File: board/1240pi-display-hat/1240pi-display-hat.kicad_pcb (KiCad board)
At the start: 2 copper layers, 34.3 x 71.1 mm, 8 parts, among them J1 Conn_02x05_Odd_Even, P208 Header, P415 Header, U1 74F126, U208 74F04, U415 74S74

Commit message: Switch hat boards from IDC ribbons to flat flex cables.
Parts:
- J1: value Conn_02x05_Odd_Even -> SFV10R-1ST; footprint Connector_PinHeader_2.54mm:PinHeader_2x05_P2.54mm_Vertical -> 0Local:Amphenol_SFV10R-1ST
- moved J1 5.64 mm to (104.0, 77.5), turned to -90 degrees
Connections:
- J1 pad 1: GND -> /~{EXT_EN}
- J1 pad 10: /~{VDRIVE} -> GND
- J1 pad 2: /~{EXT_EN} -> GND
- J1 pad 3: GND -> /PIX_CLK
- J1 pad 4: /PIX_CLK -> GND
- J1 pad 5: GND -> /VIDEO
- J1 pad 6: /VIDEO -> GND
- J1 pad 7: GND -> /~{HDRIVE}
- J1 pad 8: /~{HDRIVE} -> GND
- J1 pad 9: GND -> /~{VDRIVE}
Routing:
- net GND: track 106.3 -> 119.7 mm
- net /VIDEO: track 23.0 -> 19.2 mm, vias 0 -> 1
- net /PIX_CLK: track 30.6 -> 32.6 mm, vias 0 -> 1
- net /~{HDRIVE}: track 42.2 -> 43.8 mm
- net /~{EXT_EN}: track 41.2 -> 39.7 mm
- net /~{VDRIVE}: track 33.1 -> 33.9 mm, vias 0 -> 1
- net Net-(U1-Pad5): track 23.2 -> 23.7 mm
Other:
- board text added: "1240-Pi Display Board Mod v${REVISION}"
- board text added: "https://github.com/Elemecca/1240pi Licensed under CERN-OHL-S v2"
- board text removed: "1240-Pi Display Board Mod"
- board text removed: "GND"
- board text removed: "PIX_CLK"
- board text removed: "VIDEO"
- board text removed: "https://github.com/Elemecca/1240pi Licensed under CERN-OHL-P v2"
- board text removed: "~{EXT_EN}"
- board text removed: "~{HDRIVE}"
- board text removed: "~{VDRIVE}"

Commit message: Update board license to CERN-OHL-S v2+.
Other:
- board text added: "https://github.com/Elemecca/1240pi Licensed under CERN-OHL-S v2+"
- board text removed: "https://github.com/Elemecca/1240pi Licensed under CERN-OHL-S v2"
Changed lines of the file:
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@@
     (date "2022-05-21")
     (rev "1.0")
-    (company "© 2022 Sam Hanes, licensed under CERN-OHL-S v2")
+    (company "© 2022 Sam Hanes, licensed under CERN-OHL-S v2+")
     (comment 1 "https://github.com/Elemecca/1240pi")
-    (comment 4 "AISLER Project ID: DTIQIXZI")
   )
   (layers
@@
     (effects (font (size 1.2192 1.2192) (thickness 0.2032)) (justify left))
   )
-  (gr_text "https://github.com/Elemecca/1240pi\nLicensed under CERN-OHL-S v2" (at 125.73 59.69 -90) (layer "F.SilkS")
+  (gr_text "https://github.com/Elemecca/1240pi\nLicensed under CERN-OHL-S v2+" (at 125.73 59.69 -90) (layer "F.SilkS")
     (effects (font (size 0.8 0.8) (thickness 0.1)) (justify left))
   )

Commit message: Add bonsai logo to boards.
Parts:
- added G***: LOGO, 0Local:Symbol_Bonsai_6.7mm, F.Cu at (104.1, 94.0)
- moved REF** 51.1 mm to (104.1, 101.6)

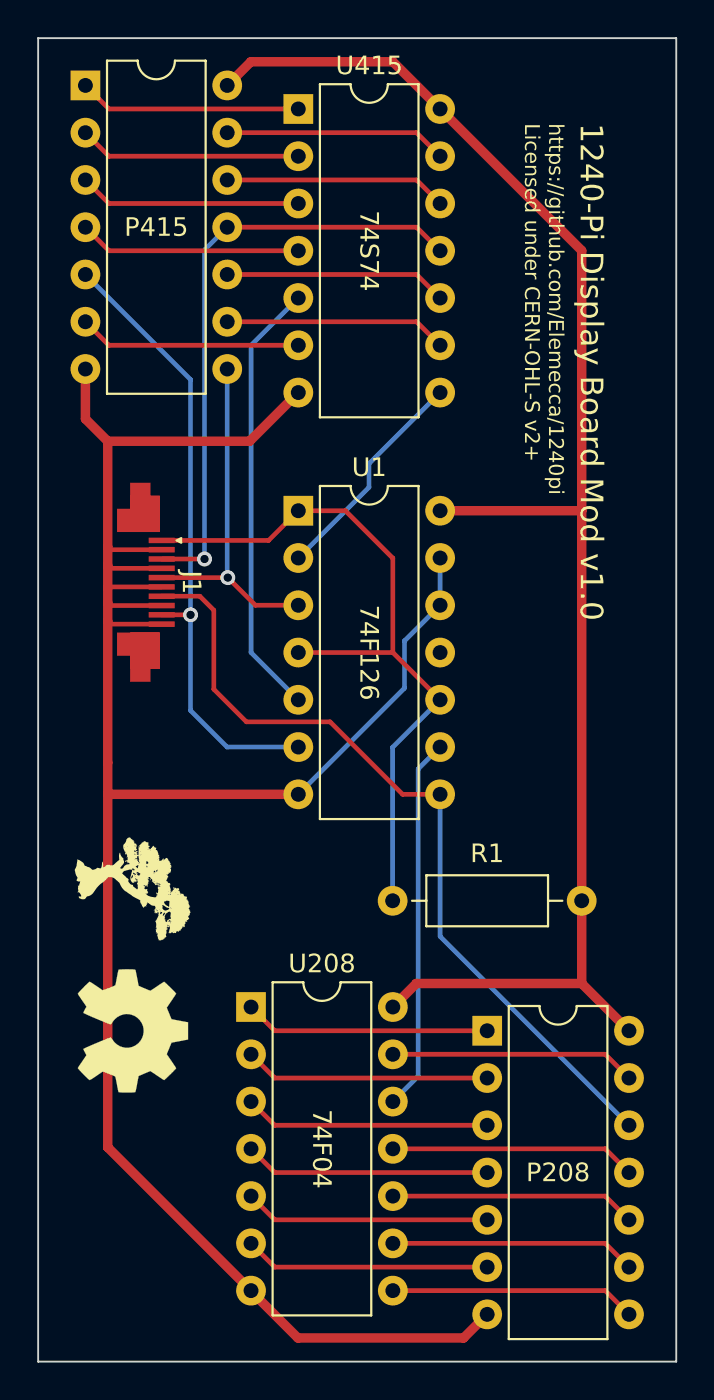
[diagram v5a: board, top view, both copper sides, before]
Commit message: Rotate sockets on hat boards 180 to match actual orientation.
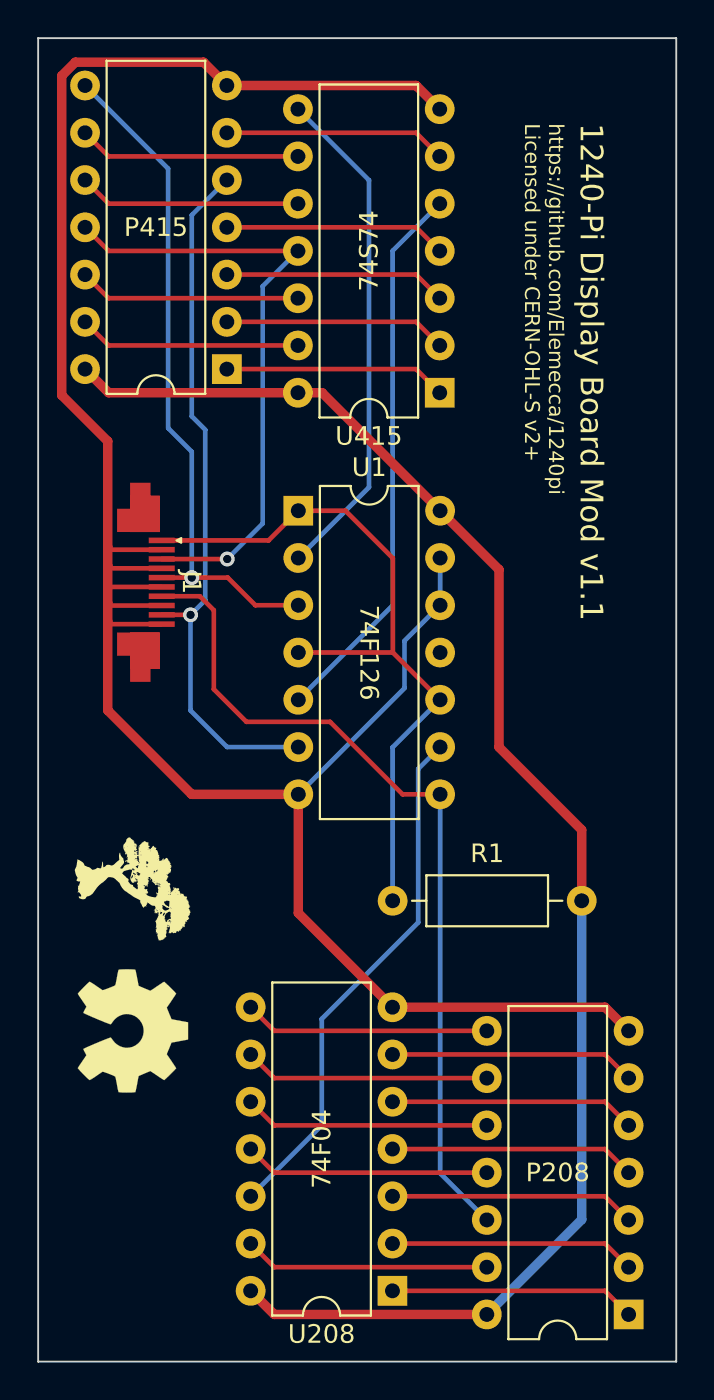
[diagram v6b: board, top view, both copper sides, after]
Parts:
- moved U208 17.0 mm to (118.1, 115.6), turned to 180 degrees
- moved U415 17.0 mm to (120.6, 67.3), turned to 180 degrees
- moved P415 17.0 mm to (109.2, 66.0), turned to 180 degrees
- moved P208 17.0 mm to (130.8, 116.8), turned to 180 degrees
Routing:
- net /VIDEO: track 19.2 -> 36.8 mm
- net Net-(U1-Pad2): track 12.1 -> 27.3 mm
- net Net-(U1-Pad9): track 20.1 -> 28.4 mm
- net GND: track 119.7 -> 126.3 mm
- net Net-(U1-Pad5): track 23.7 -> 29.8 mm
- net /~{VDRIVE}: track 33.9 -> 38.1 mm
- net /~{HDRIVE}: track 43.8 -> 45.8 mm
- net +5V: track 85.0 -> 83.9 mm
- net /PIX_CLK: track 32.6 -> 33.6 mm

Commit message: Use correct pin of U208 in display hay.
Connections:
- P208 pad 12: /~{HDRIVE} -> Net-(P208-Pad12)
- P208 pad 6: Net-(P208-Pad6) -> /~{HDRIVE}
- U208 pad 12: Net-(U1-Pad9) -> Net-(P208-Pad12)
- U208 pad 6: Net-(P208-Pad6) -> Net-(U1-Pad9)
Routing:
- net Net-(P208-Pad6): track 13.2 -> 0.00 mm
- net Net-(P208-Pad12): track 0.00 -> 13.2 mm
- net Net-(U1-Pad9): track 28.4 -> 17.6 mm
- net /~{HDRIVE}: track 45.8 -> 44.2 mm
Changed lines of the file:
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@@
   (net 10 "Net-(P208-Pad3)")
   (net 11 "Net-(P208-Pad4)")
-  (net 12 "Net-(P208-Pad5)")
-  (net 13 "Net-(P208-Pad6)")
+  (net 12 "Net-(U208-Pad5)")
+  (net 13 "Net-(P208-Pad12)")
   (net 14 "Net-(P208-Pad8)")
   (net 15 "Net-(P208-Pad9)")
@@
       (net 11 "Net-(P208-Pad4)") (pintype "output"))
     (pad "5" thru_hole oval locked (at 0 10.16 180) (size 1.6 1.6) (drill 0.8) (layers *.Cu *.Mask)
-      (net 12 "Net-(P208-Pad5)") (pintype "input"))
+      (net 12 "Net-(U208-Pad5)") (pintype "input"))
     (pad "6" thru_hole oval locked (at 0 12.7 180) (size 1.6 1.6) (drill 0.8) (layers *.Cu *.Mask)
-      (net 13 "Net-(P208-Pad6)") (pintype "output"))
+      (net 6 "/~{HDRIVE}") (pintype "output"))
     (pad "7" thru_hole oval locked (at 0 15.24 180) (size 1.6 1.6) (drill 0.8) (layers *.Cu *.Mask)
       (net 1 "GND") (pinfunction "GND") (pintype "power_in"))
@@
       (net 17 "Net-(P208-Pad11)") (pintype "input"))
     (pad "12" thru_hole oval locked (at 7.62 5.08 180) (size 1.6 1.6) (drill 0.8) (layers *.Cu *.Mask)
-      (net 6 "/~{HDRIVE}") (pintype "output"))
+      (net 13 "Net-(P208-Pad12)") (pintype "output"))
     (pad "13" thru_hole oval locked (at 7.62 2.54 180) (size 1.6 1.6) (drill 0.8) (layers *.Cu *.Mask)
       (net 18 "Net-(P208-Pad13)") (pintype "input"))
@@
       (net 11 "Net-(P208-Pad4)") (pintype "output"))
     (pad "5" thru_hole oval (at 0 10.16 180) (size 1.6 1.6) (drill 0.8) (layers *.Cu *.Mask)
-      (net 12 "Net-(P208-Pad5)") (pintype "input"))
+      (net 12 "Net-(U208-Pad5)") (pintype "input"))
     (pad "6" thru_hole oval (at 0 12.7 180) (size 1.6 1.6) (drill 0.8) (layers *.Cu *.Mask)
-      (net 13 "Net-(P208-Pad6)") (pintype "output"))
+      (net 28 "Net-(U1-Pad9)") (pintype "output"))
     (pad "7" thru_hole oval (at 0 15.24 180) (size 1.6 1.6) (drill 0.8) (layers *.Cu *.Mask)
       (net 1 "GND") (pinfunction "GND") (pintype "power_in"))
@@
       (net 17 "Net-(P208-Pad11)") (pintype "input"))
     (pad "12" thru_hole oval (at 7.62 5.08 180) (size 1.6 1.6) (drill 0.8) (layers *.Cu *.Mask)
-      (net 28 "Net-(U1-Pad9)") (pintype "output"))
+      (net 13 "Net-(P208-Pad12)") (pintype "output"))
     (pad "13" thru_hole oval (at 7.62 2.54 180) (size 1.6 1.6) (drill 0.8) (layers *.Cu *.Mask)
       (net 18 "Net-(P208-Pad13)") (pintype "input"))
@@
   (segment (start 106.045 69.215) (end 106.045 55.27) (width 0.25) (layer "B.Cu") (net 5))
   (segment (start 120.660008 88.894996) (end 118.644996 88.894996) (width 0.25) (layer "F.Cu") (net 6))
+  (segment (start 120.660008 92.720008) (end 127 99.06) (width 0.25) (layer "F.Cu") (net 6))
   (segment (start 108.5 79) (end 107.75 78.25) (width 0.25) (layer "F.Cu") (net 6))
+  (segment (start 120.660008 88.894996) (end 120.660008 92.720008) (width 0.25) (layer "F.Cu") (net 6))
+  (segment (start 127 99.06) (end 130.06865 99.06) (width 0.25) (layer "F.Cu") (net 6))
   (segment (start 108.5 83.25) (end 108.5 79) (width 0.25) (layer "F.Cu") (net 6))
+  (segment (start 132.08 101.07135) (end 132.08 102.855) (width 0.25) (layer "F.Cu") (net 6))
   (segment (start 118.644996 88.894996) (end 114.75 85) (width 0.25) (layer "F.Cu") (net 6))
   (segment (start 110.25 85) (end 108.5 83.25) (width 0.25) (layer "F.Cu") (net 6))
+  (segment (start 130.06865 99.06) (end 132.08 101.07135) (width 0.25) (layer "F.Cu") (net 6))
   (segment (start 114.75 85) (end 110.25 85) (width 0.25) (layer "F.Cu") (net 6))
+  (segment (start 132.08 102.855) (end 130.79 104.145) (width 0.25) (layer "F.Cu") (net 6))
   (segment (start 107.75 78.25) (end 105.7 78.25) (width 0.25) (layer "F.Cu") (net 6))
-  (segment (start 120.66 88.895) (end 120.66 109.255) (width 0.254) (layer "B.Cu") (net 6))
-  (segment (start 120.66 109.255) (end 123.17 111.765) (width 0.254) (layer "B.Cu") (net 6))
   (segment (start 105.7 79.25) (end 107.25 79.25) (width 0.25) (layer "F.Cu") (net 7))
   (via (at 107.25 79.25) (size 0.8) (drill 0.45) (layers "F.Cu" "B.Cu") (net 7))
@@
   (segment (start 129.519996 105.414996) (end 130.79 106.685) (width 0.25) (layer "F.Cu") (net 12))
   (segment (start 118.1 105.414996) (end 129.519996 105.414996) (width 0.25) (layer "F.Cu") (net 12))
-  (segment (start 129.519996 102.874996) (end 130.79 104.145) (width 0.25) (layer "F.Cu") (net 13))
-  (segment (start 118.1 102.874996) (end 129.519996 102.874996) (width 0.25) (layer "F.Cu") (net 13))
+  (segment (start 111.750004 111.765) (end 123.17 111.765) (width 0.25) (layer "F.Cu") (net 13))
+  (segment (start 110.48 110.494996) (end 111.750004 111.765) (width 0.25) (layer "F.Cu") (net 13))
   (segment (start 111.750004 101.605) (end 110.48 100.334996) (width 0.25) (layer "F.Cu") (net 14))
   (segment (start 123.17 101.605) (end 111.750004 101.605) (width 0.25) (layer "F.Cu") (net 14))
@@
   (segment (start 113.02 64.774996) (end 102.849996 64.774996) (width 0.25) (layer "F.Cu") (net 27))
   (segment (start 102.849996 64.774996) (end 101.58 63.505) (width 0.25) (layer "F.Cu") (net 27))
-  (segment (start 119.483489 87.531511) (end 119.483489 95.781511) (width 0.254) (layer "B.Cu") (net 28))
-  (segment (start 119.483489 87.531511) (end 120.66 86.355) (width 0.254) (layer "B.Cu") (net 28))
-  (segment (start 114.3 100.965) (end 114.3 106.674996) (width 0.254) (layer "B.Cu") (net 28))
-  (segment (start 114.3 106.674996) (end 110.48 110.494996) (width 0.254) (layer "B.Cu") (net 28))
-  (segment (start 119.483489 95.781511) (end 114.3 100.965) (width 0.254) (layer "B.Cu") (net 28))
+  (segment (start 119.483489 101.491507) (end 118.1 102.874996) (width 0.254) (layer "B.Cu") (net 28))
+  (segment (start 119.483489 87.531511) (end 119.483489 101.491507) (width 0.254) (layer "B.Cu") (net 28))
+  (segment (start 120.66 86.355) (end 119.483489 87.531511) (width 0.254) (layer "B.Cu") (net 28))
   (segment (start 116.84 55.894996) (end 113.02 52.074996) (width 0.254) (layer "B.Cu") (net 29))
   (segment (start 116.84 72.395004) (end 116.84 55.894996) (width 0.254) (layer "B.Cu") (net 29))

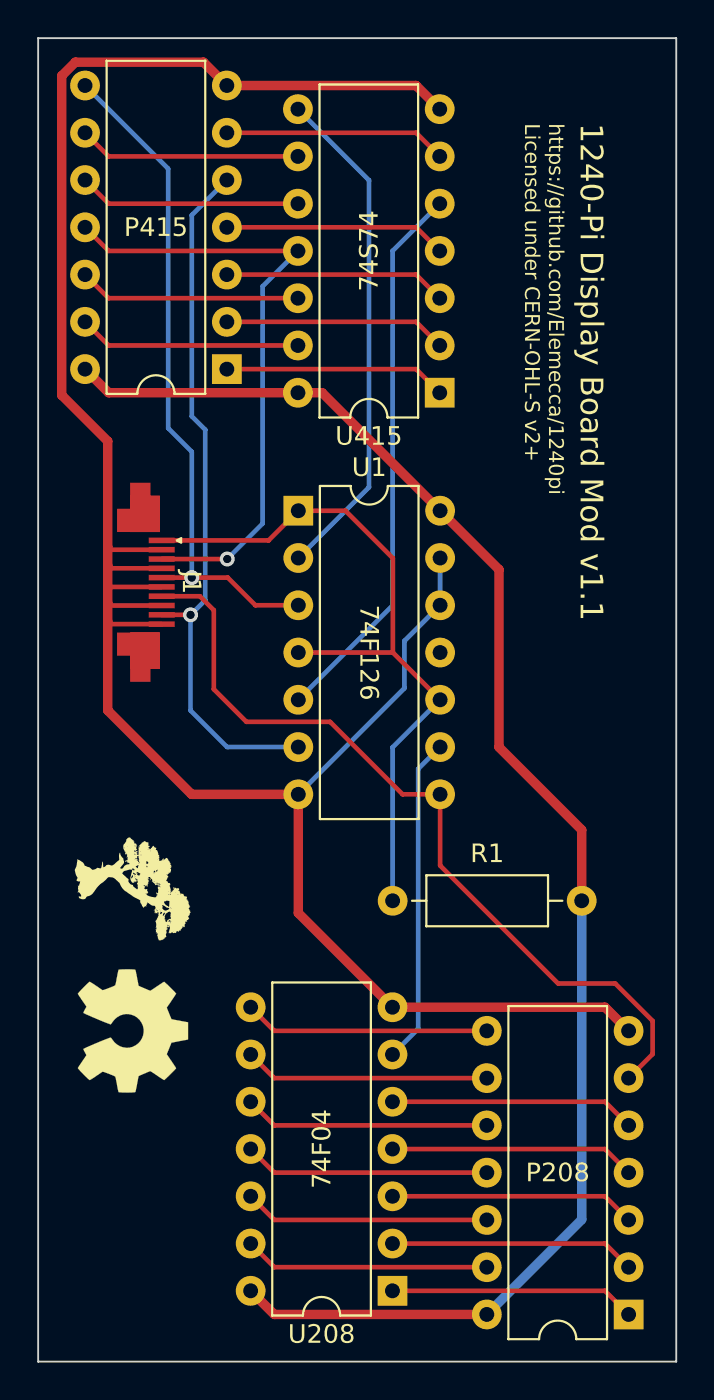
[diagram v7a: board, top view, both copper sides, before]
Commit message: Convert display board hat to 3v3.
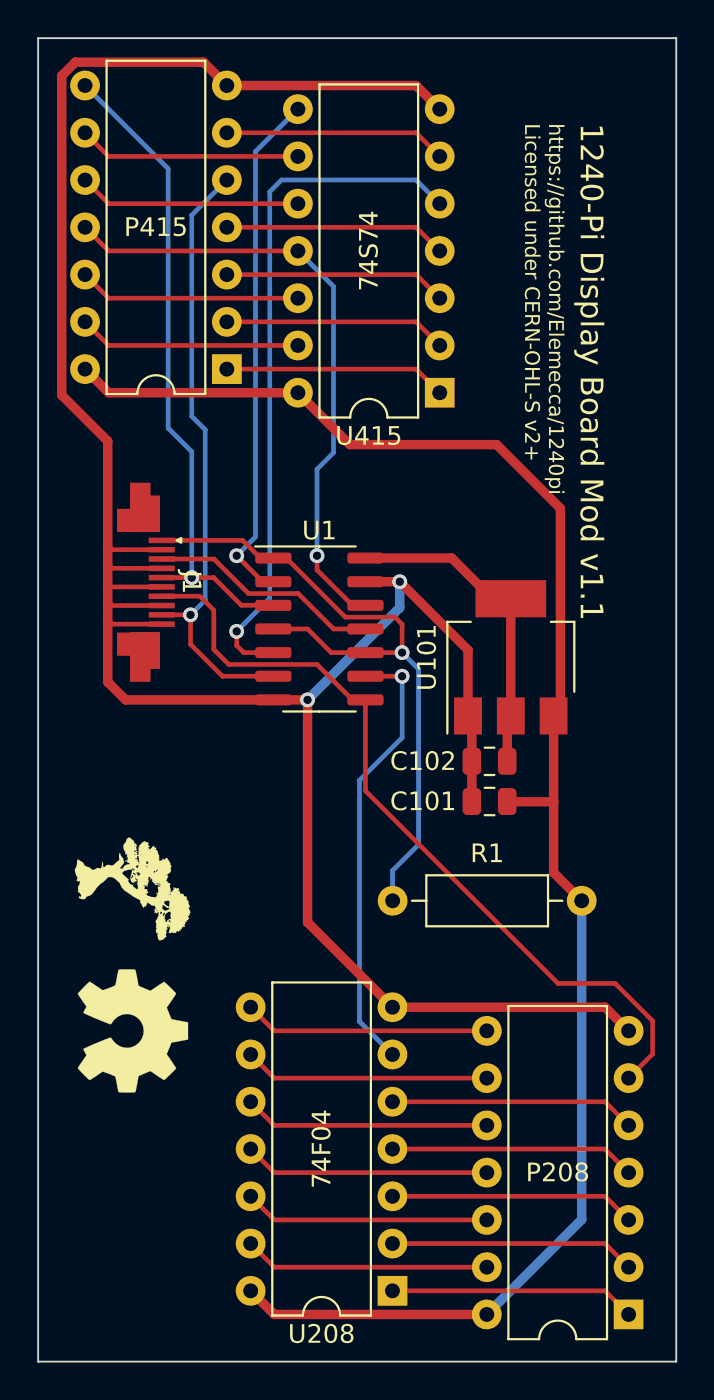
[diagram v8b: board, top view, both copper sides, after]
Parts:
- added C101: 22u, Capacitor_SMD:C_0805_2012Metric, F.Cu at (123.3, 89.3)
- added C102: 22u, Capacitor_SMD:C_0805_2012Metric, F.Cu at (123.3, 87.1)
- added U101: AP1117-33, Package_TO_SOT_SMD:SOT-223-3_TabPin2, F.Cu at (124.5, 81.5)
- U1: value 74F126 -> 74LVC126; footprint Package_DIP:DIP-14_W7.62mm -> Package_SO:SO-14_3.9x8.65mm_P1.27mm
- moved U1 6.46 mm to (114.2, 80.0)
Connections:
- J1 pad 3: /PIX_CLK -> /PIX_CLK_O
- U1 pad 11: unconnected-(U1-Pad11) -> /PIX_CLK_O
- U1 pad 12: GND -> /PIX_CLK
- U1 pad 14: +5V -> +3V3
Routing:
- net +3V3: track 0.00 -> 17.5 mm
- net /PIX_CLK_O: track 0.00 -> 12.5 mm
- net GND: track 126.3 -> 136.4 mm, vias 0 -> 2
- net Net-(U1-Pad5): track 29.8 -> 37.2 mm, vias 0 -> 1
- net +5V: track 83.9 -> 90.6 mm
- net Net-(U1-Pad9): track 17.6 -> 24.0 mm, vias 0 -> 1
- net /~{VDRIVE}: track 38.1 -> 33.1 mm
- net /~{EXT_EN}: track 39.7 -> 38.0 mm, vias 0 -> 1
- net /VIDEO: track 36.8 -> 35.4 mm
- net Net-(U1-Pad2): track 27.3 -> 27.9 mm, vias 0 -> 1
- net /~{HDRIVE}: track 44.2 -> 43.5 mm
